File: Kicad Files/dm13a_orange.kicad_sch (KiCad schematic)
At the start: 28 parts, among them U5 DM13A-GREEN, U8 DM13A-ORANGE

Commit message: VsCode firmware file + changes in the PCB layout
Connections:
- net +5V: no longer RV2.3, RV4.3
- no-connect marks 13 -> 15
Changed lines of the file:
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@@
 	)
 	(no_connect
+		(at 97.79 34.29)
+	)
+	(no_connect
 		(at 55.88 49.53)
 	)
@@
 	)
 	(no_connect
+		(at 243.84 34.29)
+	)
+	(no_connect
 		(at 55.88 62.23)
 	)
@@
 	(wire
 		(pts
-			(xy 97.79 27.94) (xy 97.79 34.29)
-		)
-		(stroke
-			(width 0)
-			(type default)
-		)
-	)
-	(wire
-		(pts
 			(xy 238.76 38.1) (xy 240.03 38.1)
 		)
@@
 	(wire
 		(pts
-			(xy 243.84 27.94) (xy 243.84 34.29)
-		)
-		(stroke
-			(width 0)
-			(type default)
-		)
-	)
-	(wire
-		(pts
 			(xy 129.54 119.38) (xy 125.73 119.38)
 		)
@@
 	(symbol
 		(lib_id "power:+5V")
-		(at 243.84 27.94 0)
-		(unit 1)
-		(exclude_from_sim no)
-		(in_bom yes)
-		(on_board yes)
-		(dnp no)
-		(fields_autoplaced yes)
-		(property "Reference" "#PWR0232"
-			(at 243.84 31.75 0)
-			(effects
-				(font
-					(size 1.27 1.27)
-				)
-				(hide yes)
-			)
-		)
-		(property "Value" "+5V"
-			(at 243.84 22.86 0)
-			(effects
-				(font
-					(size 1.27 1.27)
-				)
-			)
-		)
-		(property "Footprint" ""
-			(at 243.84 27.94 0)
-			(effects
-				(font
-					(size 1.27 1.27)
-				)
-				(hide yes)
-			)
-		)
-		(property "Datasheet" ""
-			(at 243.84 27.94 0)
-			(effects
-				(font
-					(size 1.27 1.27)
-				)
-				(hide yes)
-			)
-		)
-		(property "Description" "Power symbol creates a global label with name \"+5V\""
-			(at 243.84 27.94 0)
-			(effects
-				(font
-					(size 1.27 1.27)
-				)
-				(hide yes)
-			)
-		)
-		(pin "1"
-		)
-		(instances
-			(project "OverHead_v1"
-				(path "/b62c6a35-e532-4a7b-9786-2edcfc1d7d32/3ef15359-7692-4570-8099-43e6e5775d29"
-					(reference "#PWR0232")
-					(unit 1)
-				)
-			)
-		)
-	)
-	(symbol
-		(lib_id "power:+5V")
 		(at 29.21 119.38 90)
 		(unit 1)
@@
 					(unit 1)
 				)
-			)
-		)
-	)
-	(symbol
-		(lib_id "power:+5V")
-		(at 97.79 27.94 0)
-		(unit 1)
-		(exclude_from_sim no)
-		(in_bom yes)
-		(on_board yes)
-		(dnp no)
-		(fields_autoplaced yes)
-		(property "Reference" "#PWR0278"
-			(at 97.79 31.75 0)
-			(effects
-				(font
-					(size 1.27 1.27)
-				)
-				(hide yes)
-			)
-		)
-		(property "Value" "+5V"
-			(at 97.79 22.86 0)
-			(effects
-				(font
-					(size 1.27 1.27)
-				)
-			)
-		)
-		(property "Footprint" ""
-			(at 97.79 27.94 0)
-			(effects
-				(font
-					(size 1.27 1.27)
-				)
-				(hide yes)
-			)
-		)
-		(property "Datasheet" ""
-			(at 97.79 27.94 0)
-			(effects
-				(font
-					(size 1.27 1.27)
-				)
-				(hide yes)
-			)
-		)
-		(property "Description" "Power symbol creates a global label with name \"+5V\""
-			(at 97.79 27.94 0)
-			(effects
-				(font
-					(size 1.27 1.27)
-				)
-				(hide yes)
-			)
-		)
-		(pin "1"
-		)
-		(instances
-			(project "OverHead_v1"
-				(path "/b62c6a35-e532-4a7b-9786-2edcfc1d7d32/3ef15359-7692-4570-8099-43e6e5775d29"
-					(reference "#PWR0278")
-					(unit 1)
-				)

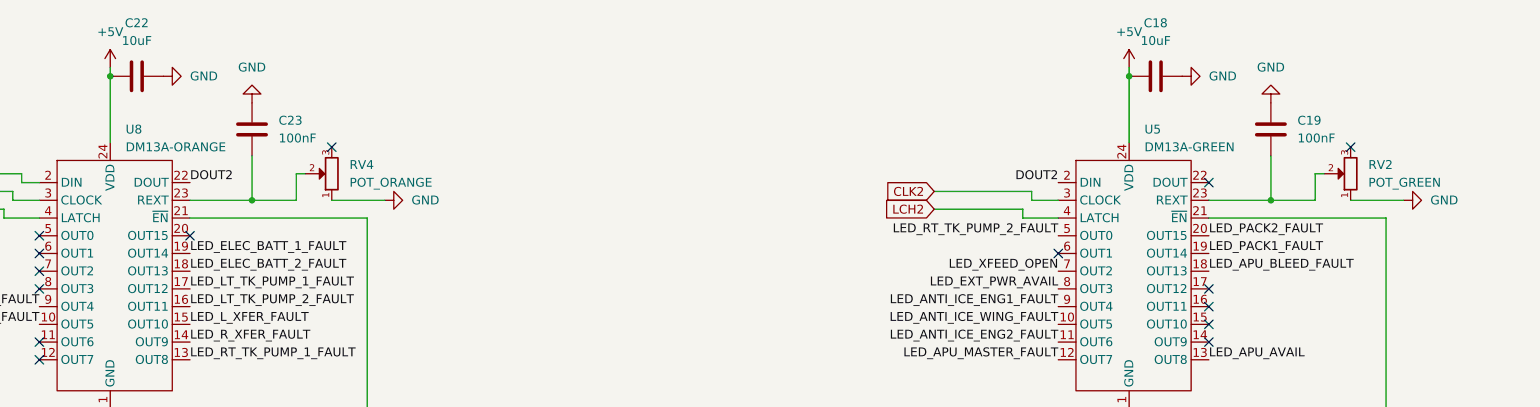
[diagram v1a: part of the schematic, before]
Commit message: Fixed some issues with the code and path on remote drive
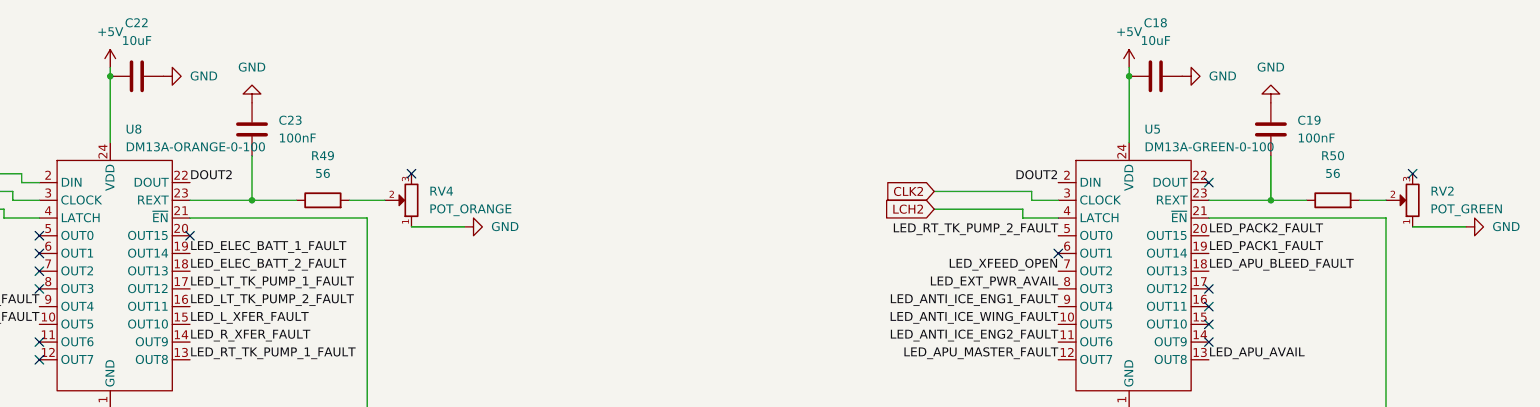
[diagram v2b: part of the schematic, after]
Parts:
- added R49, R50: 56, Resistor_SMD:R_1206_3216Metric_Pad1.30x1.75mm_HandSolder, symbol Device:R
- U5: value DM13A-GREEN -> DM13A-GREEN-0-100
- U8: value DM13A-ORANGE -> DM13A-ORANGE-0-100
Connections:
- net at C19.2, U5.23 (REXT): now also R50.1; no longer RV2.2
- net at C23.2, U8.23 (REXT): now also R49.1; no longer RV4.2
- new net: R49.2, RV4.2
- new net: R50.2, RV2.2
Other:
- moved on the sheet: RV2, RV4
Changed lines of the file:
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@@
 	)
 	(no_connect
-		(at 97.79 34.29)
+		(at 109.22 38.1)
 	)
 	(no_connect
@@
 	)
 	(no_connect
-		(at 243.84 34.29)
+		(at 252.73 38.1)
 	)
 	(no_connect
@@
 	(wire
 		(pts
-			(xy 92.71 41.91) (xy 92.71 38.1)
-		)
-		(stroke
-			(width 0)
-			(type default)
-		)
-	)
-	(wire
-		(pts
 			(xy 102.87 74.93) (xy 66.04 74.93)
 		)
@@
 	(wire
 		(pts
-			(xy 251.46 41.91) (xy 243.84 41.91)
+			(xy 260.35 45.72) (xy 252.73 45.72)
 		)
 		(stroke
@@
 	(wire
 		(pts
-			(xy 238.76 41.91) (xy 238.76 38.1)
-		)
-		(stroke
-			(width 0)
-			(type default)
-		)
-	)
-	(wire
-		(pts
 			(xy 38.1 38.1) (xy 53.34 38.1)
 		)
@@
 	(wire
 		(pts
-			(xy 238.76 38.1) (xy 240.03 38.1)
+			(xy 50.8 44.45) (xy 55.88 44.45)
 		)
 		(stroke
@@
 	(wire
 		(pts
-			(xy 50.8 44.45) (xy 55.88 44.45)
+			(xy 245.11 41.91) (xy 248.92 41.91)
 		)
 		(stroke
@@
 	(wire
 		(pts
-			(xy 105.41 41.91) (xy 97.79 41.91)
+			(xy 116.84 45.72) (xy 109.22 45.72)
 		)
 		(stroke
@@
 	(wire
 		(pts
+			(xy 232.41 41.91) (xy 237.49 41.91)
+		)
+		(stroke
+			(width 0)
+			(type default)
+		)
+	)
+	(wire
+		(pts
 			(xy 248.92 44.45) (xy 248.92 74.93)
 		)
@@
 	(wire
 		(pts
-			(xy 40.64 119.38) (xy 36.83 119.38)
+			(xy 100.33 41.91) (xy 105.41 41.91)
 		)
 		(stroke
@@
 	(wire
 		(pts
-			(xy 238.76 41.91) (xy 232.41 41.91)
+			(xy 40.64 119.38) (xy 36.83 119.38)
 		)
 		(stroke
@@
 	(wire
 		(pts
-			(xy 92.71 38.1) (xy 93.98 38.1)
-		)
-		(stroke
-			(width 0)
-			(type default)
-		)
-	)
-	(wire
-		(pts
 			(xy 129.54 107.95) (xy 125.73 107.95)
 		)
@@
 	(wire
 		(pts
-			(xy 92.71 41.91) (xy 86.36 41.91)
+			(xy 86.36 41.91) (xy 92.71 41.91)
 		)
 		(stroke
@@
 			)
 		)
-		(property "Value" "DM13A-GREEN"
+		(property "Value" "DM13A-GREEN-0-100"
 			(at 214.2841 34.29 0)
 			(effects
@@
 	(symbol
 		(lib_id "PCM_SL_Devices:potentiometer_3362P")
-		(at 97.79 38.1 90)
+		(at 109.22 41.91 90)
 		(unit 1)
 		(exclude_from_sim no)
@@
 		(fields_autoplaced yes)
 		(property "Reference" "RV4"
-			(at 100.33 36.8299 90)
+			(at 111.76 40.6399 90)
 			(effects
 				(font
@@
 		)
 		(property "Value" "POT_ORANGE"
-			(at 100.33 39.3699 90)
+			(at 111.76 43.1799 90)
 			(effects
 				(font
@@
 		)
 		(property "Footprint" "PCM_SL_Footprints:potentiometer_3362P"
-			(at 104.394 38.354 0)
+			(at 115.824 42.164 0)
 			(effects
 				(font
@@
 		)
 		(property "Datasheet" "https://www.bourns.com/data/global/pdfs/3362.pdf"
-			(at 106.426 38.354 0)
+			(at 117.856 42.164 0)
 			(effects
 				(font
@@
 		)
 		(property "Description" "potentiometer_3362P"
-			(at 97.79 38.1 0)
+			(at 109.22 41.91 0)
 			(effects
 				(font
@@
 	)
 	(symbol
+		(lib_id "Device:R")
+		(at 96.52 41.91 90)
+		(unit 1)
+		(exclude_from_sim no)
+		(in_bom yes)
+		(on_board yes)
+		(dnp no)
+		(fields_autoplaced yes)
+		(property "Reference" "R49"
+			(at 96.52 35.56 90)
+			(effects
+				(font
+					(size 1.27 1.27)
+				)
+			)
+		)
+		(property "Value" "56"
+			(at 96.52 38.1 90)
+			(effects
+				(font
+					(size 1.27 1.27)
+				)
+			)
+		)
+		(property "Footprint" "Resistor_SMD:R_1206_3216Metric_Pad1.30x1.75mm_HandSolder"
+			(at 96.52 43.688 90)
+			(effects
+				(font
+					(size 1.27 1.27)
+				)
+				(hide yes)
+			)
+		)
+		(property "Datasheet" "~"
+			(at 96.52 41.91 0)
+			(effects
+				(font
+					(size 1.27 1.27)
+				)
+				(hide yes)
+			)
+		)
+		(property "Description" "Resistor"
+			(at 96.52 41.91 0)
+			(effects
+				(font
+					(size 1.27 1.27)
+				)
+				(hide yes)
+			)
+		)
+		(pin "1"
+		)
+		(pin "2"
+		)
+		(instances
+			(project ""
+				(path "/b62c6a35-e532-4a7b-9786-2edcfc1d7d32/3ef15359-7692-4570-8099-43e6e5775d29"
+					(reference "R49")
+					(unit 1)
+				)
+			)
+		)
+	)
+	(symbol
 		(lib_id "power:+5V")
 		(at 74.93 153.67 90)
@@
 	(symbol
 		(lib_id "PCM_SL_Devices:potentiometer_3362P")
-		(at 243.84 38.1 90)
+		(at 252.73 41.91 90)
 		(unit 1)
 		(exclude_from_sim no)
@@
 		(fields_autoplaced yes)
 		(property "Reference" "RV2"
-			(at 246.38 36.8299 90)
+			(at 255.27 40.6399 90)
 			(effects
 				(font
@@
 		)
 		(property "Value" "POT_GREEN"
-			(at 246.38 39.3699 90)
+			(at 255.27 43.1799 90)
 			(effects
 				(font
@@
 		)
 		(property "Footprint" "PCM_SL_Footprints:potentiometer_3362P"
-			(at 250.444 38.354 0)
+			(at 259.334 42.164 0)
 			(effects
 				(font
@@
 		)
 		(property "Datasheet" "https://www.bourns.com/data/global/pdfs/3362.pdf"
-			(at 252.476 38.354 0)
+			(at 261.366 42.164 0)
 			(effects
 				(font
@@
 		)
 		(property "Description" "potentiometer_3362P"
-			(at 243.84 38.1 0)
+			(at 252.73 41.91 0)
 			(effects
 				(font
@@
 	)
 	(symbol
+		(lib_id "Device:R")
+		(at 241.3 41.91 90)
+		(unit 1)
+		(exclude_from_sim no)
+		(in_bom yes)
+		(on_board yes)
+		(dnp no)
+		(fields_autoplaced yes)
+		(property "Reference" "R50"
+			(at 241.3 35.56 90)
+			(effects
+				(font
+					(size 1.27 1.27)
+				)
+			)
+		)
+		(property "Value" "56"
+			(at 241.3 38.1 90)
+			(effects
+				(font
+					(size 1.27 1.27)
+				)
+			)
+		)
+		(property "Footprint" "Resistor_SMD:R_1206_3216Metric_Pad1.30x1.75mm_HandSolder"
+			(at 241.3 43.688 90)
+			(effects
+				(font
+					(size 1.27 1.27)
+				)
+				(hide yes)
+			)
+		)
+		(property "Datasheet" "~"
+			(at 241.3 41.91 0)
+			(effects
+				(font
+					(size 1.27 1.27)
+				)
+				(hide yes)
+			)
+		)
+		(property "Description" "Resistor"
+			(at 241.3 41.91 0)
+			(effects
+				(font
+					(size 1.27 1.27)
+				)
+				(hide yes)
+			)
+		)
+		(pin "1"
+		)
+		(pin "2"
+		)
+		(instances
+			(project "OverHead_v1"
+				(path "/b62c6a35-e532-4a7b-9786-2edcfc1d7d32/3ef15359-7692-4570-8099-43e6e5775d29"
+					(reference "R50")
+					(unit 1)
+				)
+			)
+		)
+	)
+	(symbol
 		(lib_id "Device:LED")
 		(at 77.47 142.24 180)
@@
 			)
 		)
-		(property "Value" "DM13A-ORANGE"
+		(property "Value" "DM13A-ORANGE-0-100"
 			(at 68.2341 34.29 0)
 			(effects
@@
 	(symbol
 		(lib_id "power:GND")
-		(at 251.46 41.91 90)
+		(at 260.35 45.72 90)
 		(unit 1)
 		(exclude_from_sim no)
@@
 		(fields_autoplaced yes)
 		(property "Reference" "#PWR0233"
-			(at 257.81 41.91 0)
+			(at 266.7 45.72 0)
 			(effects
 				(font
@@
 		)
 		(property "Value" "GND"
-			(at 255.27 41.9099 90)
+			(at 264.16 45.7199 90)
 			(effects
 				(font
@@
 		)
 		(property "Footprint" ""
-			(at 251.46 41.91 0)
+			(at 260.35 45.72 0)
 			(effects
 				(font
@@
 		)
 		(property "Datasheet" ""
-			(at 251.46 41.91 0)
+			(at 260.35 45.72 0)
 			(effects
 				(font
@@
 		)
 		(property "Description" "Power symbol creates a global label with name \"GND\" , ground"
-			(at 251.46 41.91 0)
+			(at 260.35 45.72 0)
 			(effects
 				(font
@@
 	(symbol
 		(lib_id "power:GND")
-		(at 105.41 41.91 90)
+		(at 116.84 45.72 90)
 		(unit 1)
 		(exclude_from_sim no)
@@
 		(fields_autoplaced yes)
 		(property "Reference" "#PWR0279"
-			(at 111.76 41.91 0)
+			(at 123.19 45.72 0)
 			(effects
 				(font
@@
 		)
 		(property "Value" "GND"
-			(at 109.22 41.9099 90)
+			(at 120.65 45.7199 90)
 			(effects
 				(font
@@
 		)
 		(property "Footprint" ""
-			(at 105.41 41.91 0)
+			(at 116.84 45.72 0)
 			(effects
 				(font
@@
 		)
 		(property "Datasheet" ""
-			(at 105.41 41.91 0)
+			(at 116.84 45.72 0)
 			(effects
 				(font
@@
 		)
 		(property "Description" "Power symbol creates a global label with name \"GND\" , ground"
-			(at 105.41 41.91 0)
+			(at 116.84 45.72 0)
 			(effects
 				(font

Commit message: New STL files for APU OVHD element, other coming in the next few weeks
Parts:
- D1, D108, D128, D178, D183, D184, D185, D188, D190, D2, D3, D50, D51, D52, D75, D77, D87, D89, D91, D99: footprint LED_THT:LED_Rectangular_W3.9mm_H1.8mm_FlatTop -> PCM_LED_THT_AKL:LED_Rectangular_W3.9mm_H1.8mm_FlatTop
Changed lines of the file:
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@@
 (kicad_sch
-	(version 20231120)
+	(version 20250114)
 	(generator "eeschema")
-	(generator_version "8.0")
+	(generator_version "9.0")
 	(paper "A4")
 	(junction
@@
 	(label "LED_RT_TK_PUMP_2_FAULT"
 		(at 129.54 153.67 0)
-		(fields_autoplaced yes)
 		(effects
 			(font
@@
 	(label "LED_ELEC_BATT_1_FAULT"
 		(at 77.47 49.53 0)
-		(fields_autoplaced yes)
 		(effects
 			(font
@@
 	(label "LED_RT_TK_PUMP_2_FAULT"
 		(at 201.93 46.99 180)
-		(fields_autoplaced yes)
 		(effects
 			(font
@@
 	(label "LED_ANTI_ICE_ENG1_FAULT"
 		(at 201.93 57.15 180)
-		(fields_autoplaced yes)
 		(effects
 			(font
@@
 	(label "LED_EXT_PWR_AVAIL"
 		(at 201.93 54.61 180)
-		(fields_autoplaced yes)
 		(effects
 			(font
@@
 	(label "LED_EXT_PWR_AVAIL"
 		(at 41.91 165.1 0)
-		(fields_autoplaced yes)
 		(effects
 			(font
@@
 	(label "LED_R_XFER_FAULT"
 		(at 77.47 62.23 0)
-		(fields_autoplaced yes)
 		(effects
 			(font
@@
 	(label "LED_ANTI_ICE_ENG2_FAULT"
 		(at 201.93 62.23 180)
-		(fields_autoplaced yes)
 		(effects
 			(font
@@
 	(label "LED_PACK2_FAULT"
 		(at 85.09 119.38 0)
-		(fields_autoplaced yes)
 		(effects
 			(font
@@
 	(label "LED_APU_BLEED_FAULT"
 		(at 223.52 52.07 0)
-		(fields_autoplaced yes)
 		(effects
 			(font
@@
 	(label "LED_GPWS_SYS_FAULT"
 		(at 55.88 59.69 180)
-		(fields_autoplaced yes)
 		(effects
 			(font
@@
 	(label "LED_L_XFER_FAULT"
 		(at 129.54 119.38 0)
-		(fields_autoplaced yes)
 		(effects
 			(font
@@
 	(label "DOUT2"
 		(at 201.93 39.37 180)
-		(fields_autoplaced yes)
 		(effects
 			(font
@@
 	(label "LED_L_XFER_FAULT"
 		(at 77.47 59.69 0)
-		(fields_autoplaced yes)
 		(effects
 			(font
@@
 	(label "LED_RT_TK_PUMP_1_FAULT"
 		(at 77.47 64.77 0)
-		(fields_autoplaced yes)
 		(effects
 			(font
@@
 	(label "LED_ANTI_ICE_WING_FAULT"
 		(at 201.93 59.69 180)
-		(fields_autoplaced yes)
 		(effects
 			(font
@@
 	(label "LED_ANTI_ICE_ENG2_FAULT"
 		(at 40.64 153.67 0)
-		(fields_autoplaced yes)
 		(effects
 			(font
@@
 	(label "LED_XFEED_OPEN"
 		(at 87.63 165.1 0)
-		(fields_autoplaced yes)
 		(effects
 			(font
@@
 	(label "LED_GPWS_SYS_FAULT"
 		(at 40.64 119.38 0)
-		(fields_autoplaced yes)
 		(effects
 			(font
@@
 	(label "LED_LT_TK_PUMP_1_FAULT"
 		(at 77.47 54.61 0)
-		(fields_autoplaced yes)
 		(effects
 			(font
@@
 	(label "LED_LT_TK_PUMP_2_FAULT"
 		(at 77.47 57.15 0)
-		(fields_autoplaced yes)
 		(effects
 			(font
@@
 	(label "DOUT2"
 		(at 77.47 39.37 0)
-		(fields_autoplaced yes)
 		(effects
 			(font
@@
 	(label "LED_GPWS_TERR_FAULT"
 		(at 55.88 57.15 180)
-		(fields_autoplaced yes)
 		(effects
 			(font
@@
 	(label "LED_APU_AVAIL"
 		(at 87.63 153.67 0)
-		(fields_autoplaced yes)
 		(effects
 			(font
@@
 	(label "LED_APU_BLEED_FAULT"
 		(at 83.82 96.52 0)
-		(fields_autoplaced yes)
 		(effects
 			(font
@@
 	(label "LED_PACK2_FAULT"
 		(at 223.52 46.99 0)
-		(fields_autoplaced yes)
 		(effects
 			(font
@@
 	(label "LED_R_XFER_FAULT"
 		(at 129.54 130.81 0)
-		(fields_autoplaced yes)
 		(effects
 			(font
@@
 	(label "LED_ELEC_BATT_1_FAULT"
 		(at 85.09 130.81 0)
-		(fields_autoplaced yes)
 		(effects
 			(font
@@
 	(label "LED_GPWS_TERR_FAULT"
 		(at 41.91 107.95 0)
-		(fields_autoplaced yes)
 		(effects
 			(font
@@
 	(label "LED_APU_MASTER_FAULT"
 		(at 201.93 64.77 180)
-		(fields_autoplaced yes)
 		(effects
 			(font
@@
 	(label "LED_ANTI_ICE_ENG1_FAULT"
 		(at 40.64 130.81 0)
-		(fields_autoplaced yes)
 		(effects
 			(font
@@
 	(label "LED_RT_TK_PUMP_1_FAULT"
 		(at 129.54 142.24 0)
-		(fields_autoplaced yes)
 		(effects
 			(font
@@
 	(label "LED_ELEC_BATT_2_FAULT"
 		(at 77.47 52.07 0)
-		(fields_autoplaced yes)
 		(effects
 			(font
@@
 	(label "LED_PACK1_FAULT"
 		(at 223.52 49.53 0)
-		(fields_autoplaced yes)
 		(effects
 			(font
@@
 	(label "LED_ELEC_BATT_2_FAULT"
 		(at 85.09 142.24 0)
-		(fields_autoplaced yes)
 		(effects
 			(font
@@
 	(label "LED_PACK1_FAULT"
 		(at 83.82 107.95 0)
-		(fields_autoplaced yes)
 		(effects
 			(font
@@
 	(label "LED_APU_MASTER_FAULT"
 		(at 40.64 96.52 0)
-		(fields_autoplaced yes)
 		(effects
 			(font
@@
 	(label "LED_LT_TK_PUMP_1_FAULT"
 		(at 129.54 96.52 0)
-		(fields_autoplaced yes)
 		(effects
 			(font
@@
 	(label "LED_ANTI_ICE_WING_FAULT"
 		(at 40.64 142.24 0)
-		(fields_autoplaced yes)
 		(effects
 			(font
@@
 	(label "LED_APU_AVAIL"
 		(at 223.52 64.77 0)
-		(fields_autoplaced yes)
 		(effects
 			(font
@@
 	(label "LED_LT_TK_PUMP_2_FAULT"
 		(at 129.54 107.95 0)
-		(fields_autoplaced yes)
 		(effects
 			(font
@@
 	(label "LED_XFEED_OPEN"
 		(at 201.93 52.07 180)
-		(fields_autoplaced yes)
 		(effects
 			(font
@@
 			)
 		)
-		(property "Footprint" "LED_THT:LED_Rectangular_W3.9mm_H1.8mm_FlatTop"
+		(property "Footprint" "PCM_LED_THT_AKL:LED_Rectangular_W3.9mm_H1.8mm_FlatTop"
 			(at 121.92 96.52 0)
 			(effects
@@
 			)
 		)
-		(property "Footprint" "LED_THT:LED_Rectangular_W3.9mm_H1.8mm_FlatTop"
+		(property "Footprint" "PCM_LED_THT_AKL:LED_Rectangular_W3.9mm_H1.8mm_FlatTop"
 			(at 33.02 130.81 0)
 			(effects
@@
 			)
 		)
-		(property "Footprint" "LED_THT:LED_Rectangular_W3.9mm_H1.8mm_FlatTop"
+		(property "Footprint" "PCM_LED_THT_AKL:LED_Rectangular_W3.9mm_H1.8mm_FlatTop"
 			(at 121.92 107.95 0)
 			(effects
@@
 			)
 		)
-		(property "Footprint" "LED_THT:LED_Rectangular_W3.9mm_H1.8mm_FlatTop"
+		(property "Footprint" "PCM_LED_THT_AKL:LED_Rectangular_W3.9mm_H1.8mm_FlatTop"
 			(at 121.92 130.81 0)
 			(effects
@@
 			)
 		)
-		(property "Footprint" "LED_THT:LED_Rectangular_W3.9mm_H1.8mm_FlatTop"
+		(property "Footprint" "PCM_LED_THT_AKL:LED_Rectangular_W3.9mm_H1.8mm_FlatTop"
 			(at 33.02 96.52 0)
 			(effects
@@
 			)
 		)
-		(property "Footprint" "LED_THT:LED_Rectangular_W3.9mm_H1.8mm_FlatTop"
+		(property "Footprint" "PCM_LED_THT_AKL:LED_Rectangular_W3.9mm_H1.8mm_FlatTop"
 			(at 76.2 96.52 0)
 			(effects
@@
 			)
 		)
-		(property "Footprint" "LED_THT:LED_Rectangular_W3.9mm_H1.8mm_FlatTop"
+		(property "Footprint" "PCM_LED_THT_AKL:LED_Rectangular_W3.9mm_H1.8mm_FlatTop"
 			(at 121.92 119.38 0)
 			(effects
@@
 			)
 		)
-		(property "Footprint" "LED_THT:LED_Rectangular_W3.9mm_H1.8mm_FlatTop"
+		(property "Footprint" "PCM_LED_THT_AKL:LED_Rectangular_W3.9mm_H1.8mm_FlatTop"
 			(at 77.47 130.81 0)
 			(effects
@@
 			)
 		)
-		(property "Footprint" "LED_THT:LED_Rectangular_W3.9mm_H1.8mm_FlatTop"
+		(property "Footprint" "PCM_LED_THT_AKL:LED_Rectangular_W3.9mm_H1.8mm_FlatTop"
 			(at 78.74 165.1 0)
 			(effects
@@
 			)
 		)
-		(property "Footprint" "LED_THT:LED_Rectangular_W3.9mm_H1.8mm_FlatTop"
+		(property "Footprint" "PCM_LED_THT_AKL:LED_Rectangular_W3.9mm_H1.8mm_FlatTop"
 			(at 77.47 142.24 0)
 			(effects
@@
 			)
 		)
-		(property "Footprint" "LED_THT:LED_Rectangular_W3.9mm_H1.8mm_FlatTop"
+		(property "Footprint" "PCM_LED_THT_AKL:LED_Rectangular_W3.9mm_H1.8mm_FlatTop"
 			(at 77.47 119.38 0)
 			(effects
@@
 			)
 		)
-		(property "Footprint" "LED_THT:LED_Rectangular_W3.9mm_H1.8mm_FlatTop"
+		(property "Footprint" "PCM_LED_THT_AKL:LED_Rectangular_W3.9mm_H1.8mm_FlatTop"
 			(at 76.2 107.95 0)
 			(effects
@@
 			)
 		)
-		(property "Footprint" "LED_THT:LED_Rectangular_W3.9mm_H1.8mm_FlatTop"
+		(property "Footprint" "PCM_LED_THT_AKL:LED_Rectangular_W3.9mm_H1.8mm_FlatTop"
 			(at 33.02 119.38 0)
 			(effects
@@
 			)
 		)
-		(property "Footprint" "LED_THT:LED_Rectangular_W3.9mm_H1.8mm_FlatTop"
+		(property "Footprint" "PCM_LED_THT_AKL:LED_Rectangular_W3.9mm_H1.8mm_FlatTop"
 			(at 33.02 165.1 0)
 			(effects
@@
 			)
 		)
-		(property "Footprint" "LED_THT:LED_Rectangular_W3.9mm_H1.8mm_FlatTop"
+		(property "Footprint" "PCM_LED_THT_AKL:LED_Rectangular_W3.9mm_H1.8mm_FlatTop"
 			(at 33.02 153.67 0)
 			(effects
@@
 			)
 		)
-		(property "Footprint" "LED_THT:LED_Rectangular_W3.9mm_H1.8mm_FlatTop"
+		(property "Footprint" "PCM_LED_THT_AKL:LED_Rectangular_W3.9mm_H1.8mm_FlatTop"
 			(at 33.02 142.24 0)
 			(effects
@@
 			)
 		)
-		(property "Footprint" "LED_THT:LED_Rectangular_W3.9mm_H1.8mm_FlatTop"
+		(property "Footprint" "PCM_LED_THT_AKL:LED_Rectangular_W3.9mm_H1.8mm_FlatTop"
 			(at 33.02 107.95 0)
 			(effects
@@
 			)
 		)
-		(property "Footprint" "LED_THT:LED_Rectangular_W3.9mm_H1.8mm_FlatTop"
+		(property "Footprint" "PCM_LED_THT_AKL:LED_Rectangular_W3.9mm_H1.8mm_FlatTop"
 			(at 78.74 153.67 0)
 			(effects
@@
 			)
 		)
-		(property "Footprint" "LED_THT:LED_Rectangular_W3.9mm_H1.8mm_FlatTop"
+		(property "Footprint" "PCM_LED_THT_AKL:LED_Rectangular_W3.9mm_H1.8mm_FlatTop"
 			(at 121.92 153.67 0)
 			(effects
@@
 			)
 		)
-		(property "Footprint" "LED_THT:LED_Rectangular_W3.9mm_H1.8mm_FlatTop"
+		(property "Footprint" "PCM_LED_THT_AKL:LED_Rectangular_W3.9mm_H1.8mm_FlatTop"
 			(at 121.92 142.24 0)
 			(effects
